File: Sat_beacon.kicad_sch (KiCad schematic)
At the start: 131 parts, among them IC1 LMX2581ESQE_NOPB, IC2 LMX2581ESQE_NOPB, J1 Conn_01x05_Pin, J2 Conn_01x05_Pin, J3 Conn_01x03_Pin, J4 MMCX, J5 MMCX, Q1 BC817-40, Q2 BC817-40, Q3 BC817-40, Q4 BC817-40, SW1 SW_SPDT_312, SW2 SW_Omron_B3FS, SW3 SW_Omron_B3FS, SW4 SW_Omron_B3FS, SW5 SW_Omron_B3FS, U1 STM32C011F6Px, U2 LD1117DT33, U3 LD1117DT33, U4 1720BL15B0050002E, U5 1720BL15B0050002E, U6 LD1117DT33, U7 STM32C031C6Tx, Y1 FT2MHUPM10.0-T1

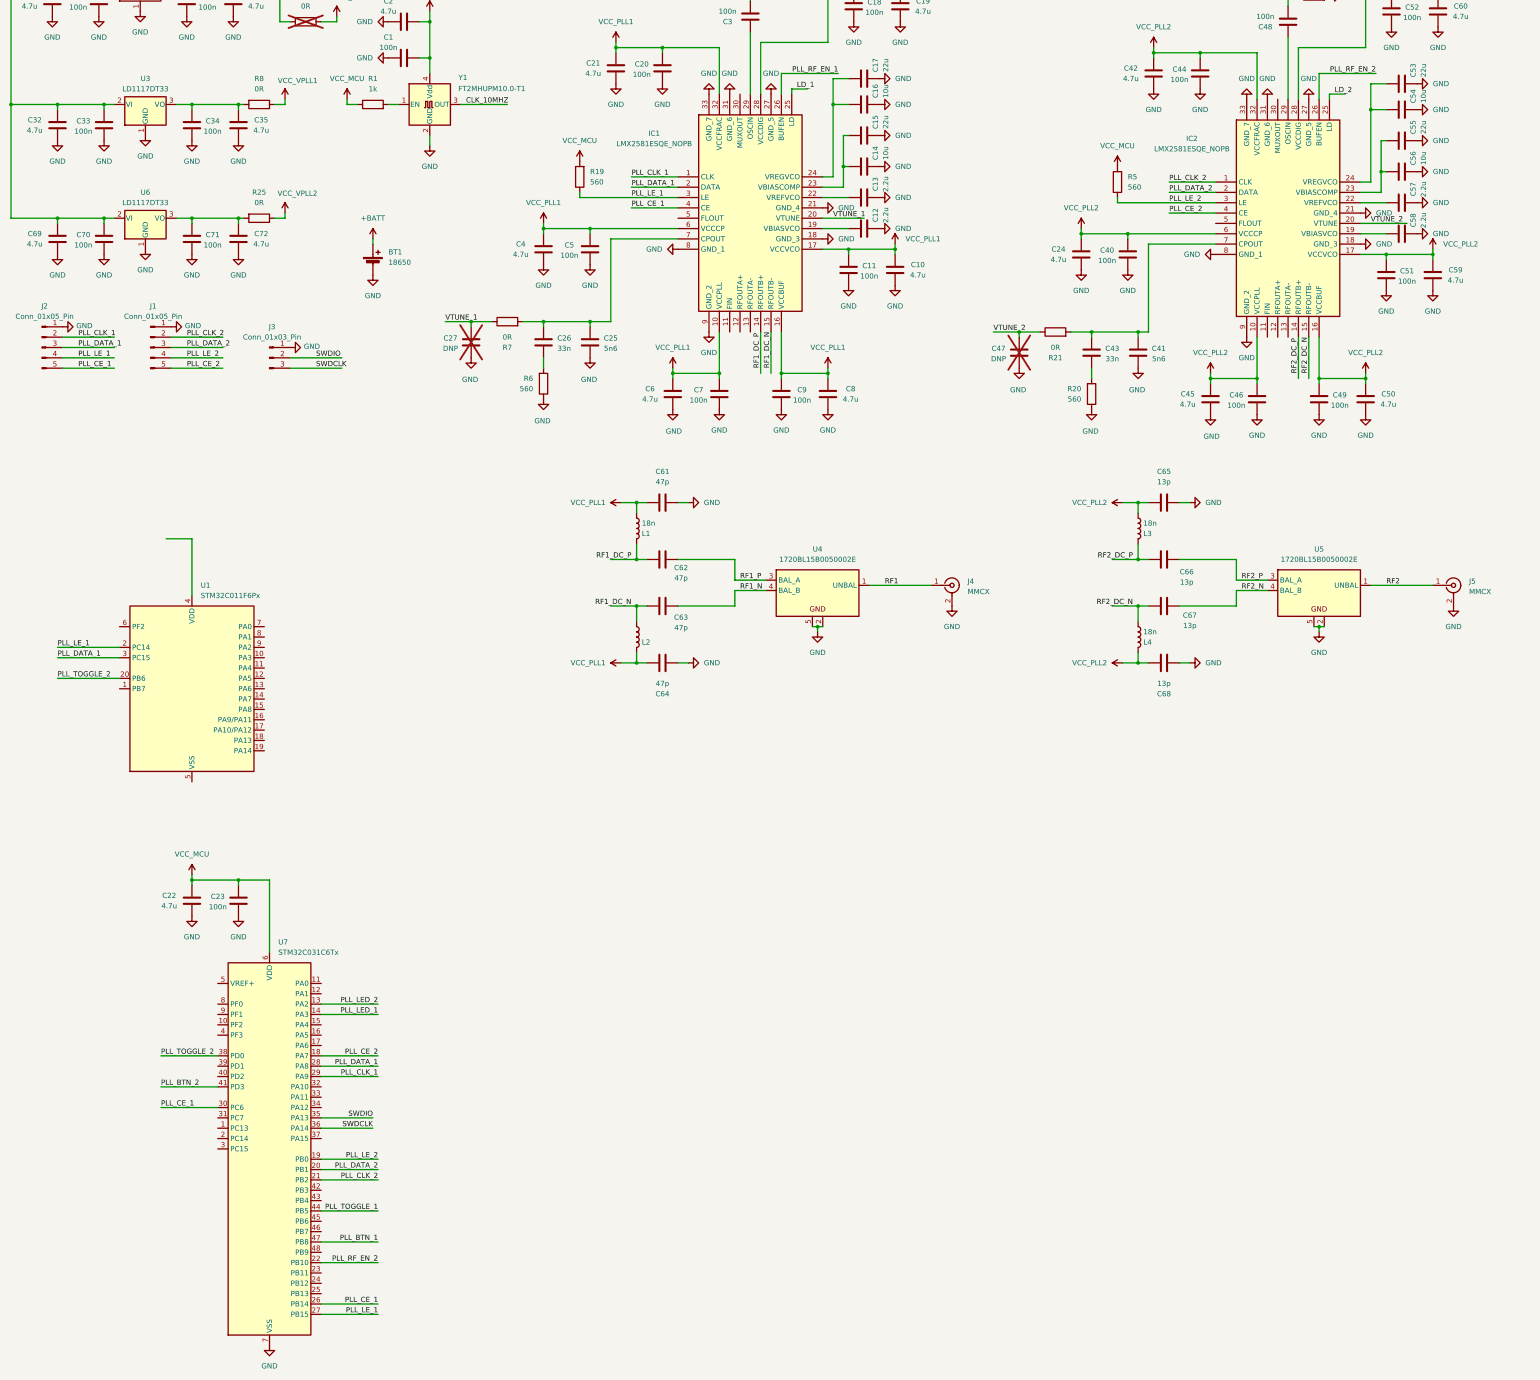
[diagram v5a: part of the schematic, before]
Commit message: Group and place components on PCB, two PLL caps removed, swapped RF lines
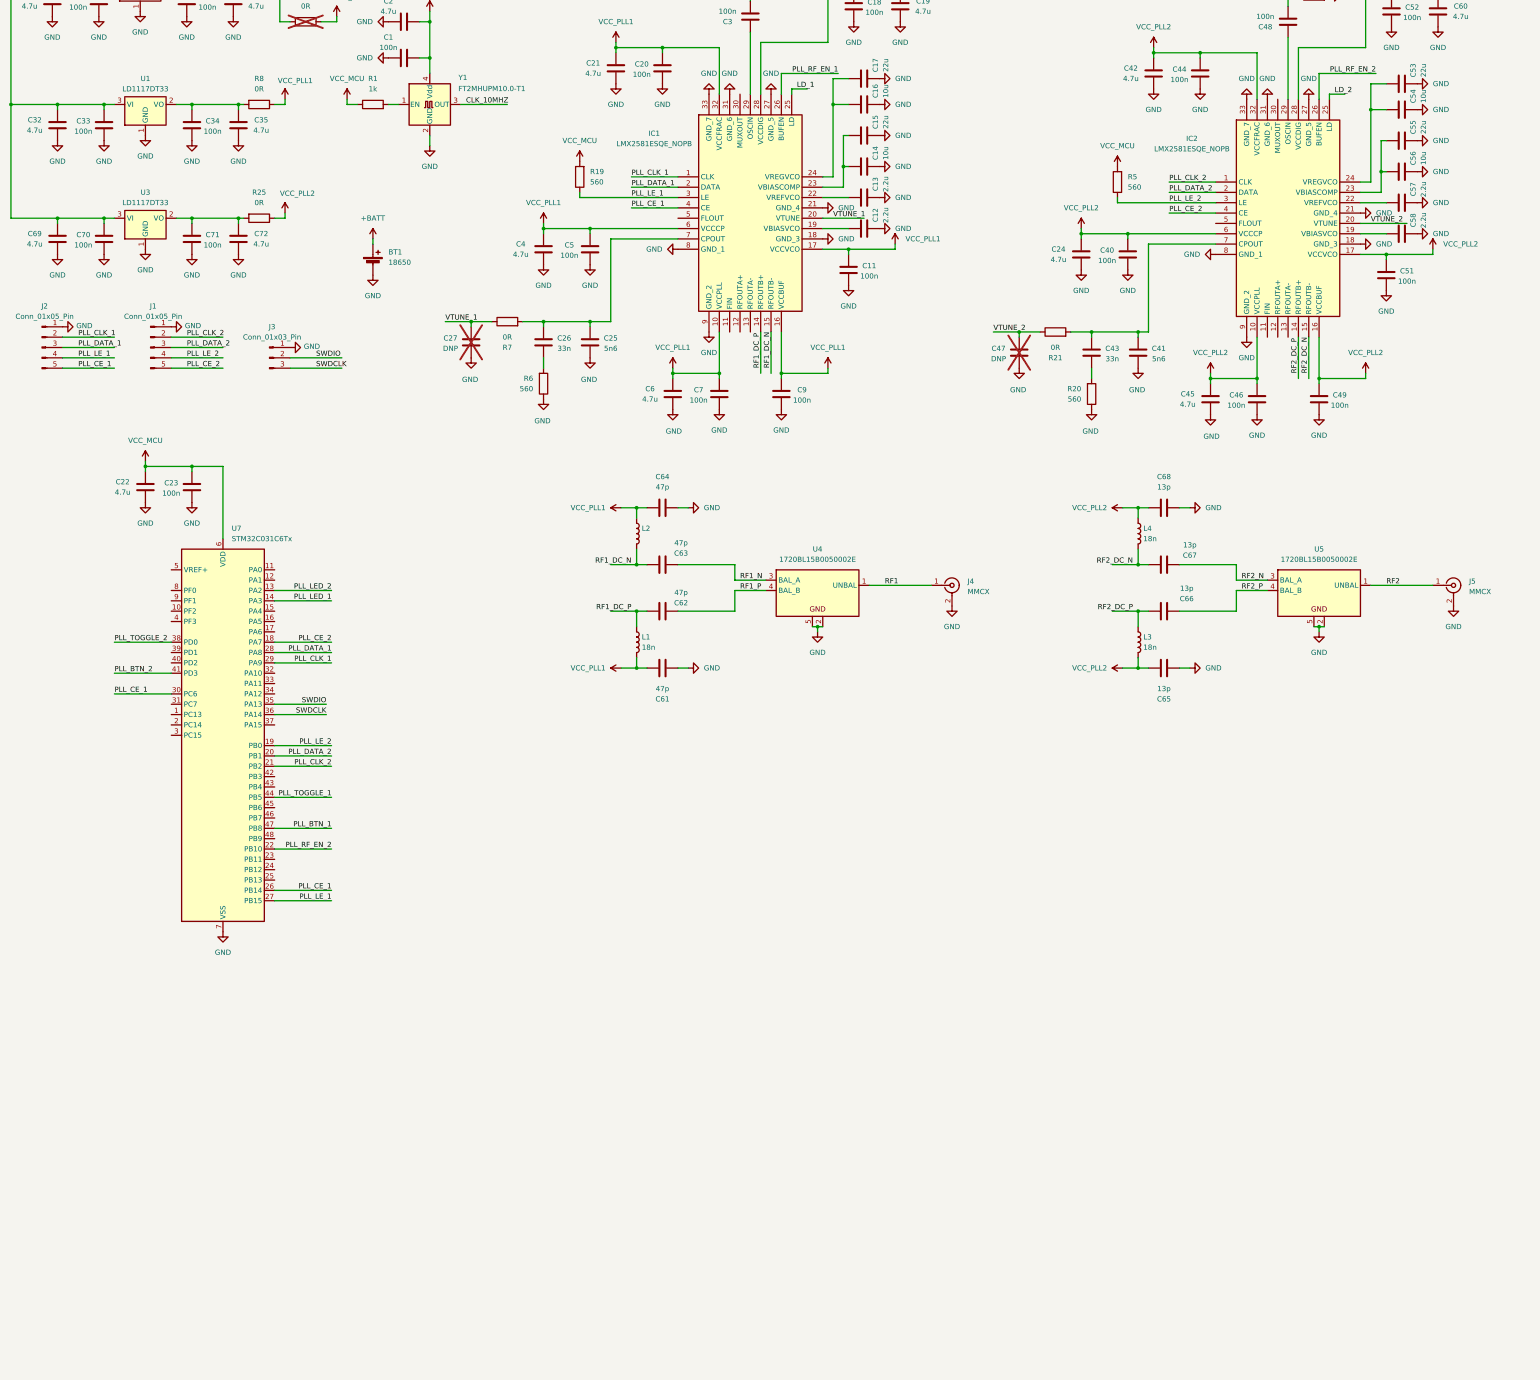
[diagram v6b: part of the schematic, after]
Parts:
- removed C10, C50, C59, C8: 4.7u, Capacitor_SMD:C_0805_2012Metric, symbol Device:C
- removed U1: STM32C011F6Px, Package_SO:TSSOP-20_4.4x6.5mm_P0.65mm, symbol MCU_ST_STM32C0:STM32C011F6Px
- removed U3, U6: LD1117DT33, Package_TO_SOT_THT:TO-220-3_Vertical, symbol Regulator_Linear:MCP1700x-330xxMB
- added U1, U3: LD1117DT33, Package_TO_SOT_SMD:TO-252-3_TabPin2, symbol Regulator_Linear:LD1117V33
- U2: footprint Package_TO_SOT_THT:TO-220-3_Vertical -> Package_TO_SOT_SMD:TO-252-3_TabPin2
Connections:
- net VCC_VPLL1 is gone; now on net VCC_PLL1: R8.1
- net VCC_VPLL2 is gone; now on net VCC_PLL2: R25.1
- net GND: now also U1.1 (GND), U3.1 (GND)
- net RF1_N: now also U4.3 (BAL_A); no longer U4.4 (BAL_B)
- net RF1_P: now also U4.4 (BAL_B); no longer U4.3 (BAL_A)
- net RF2_N: now also U5.3 (BAL_A); no longer U5.4 (BAL_B)
- net RF2_P: now also U5.4 (BAL_B); no longer U5.3 (BAL_A)
- net at C28.2, C29.2, C32.2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: now also U1.3 (VI), U3.3 (VI)
- net at C71.2, C72.2, R25.2: now also U3.2 (VO)
- net at C34.2, C35.2, R8.2: now also U1.2 (VO)
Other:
- moved on the sheet: C22, C23, C61, C62, C63, C64, C65, C66, C67, C68, L1, L2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

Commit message: MUXout added, LEDs swapped (SCH only)
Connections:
- net PLL_CE_1: no longer U7.30 (PC6)
- net PLL_LED_1: now also R18.1, U7.13 (PA2); no longer R16.1, U7.14 (PA3)
- net PLL_LED_2: now also R16.1, U7.14 (PA3); no longer R18.1, U7.13 (PA2)
- net PLL_RF_EN_1: now also U7.31 (PC7)
- net PLL_RF_EN_2: now also U7.23 (PB11); no longer U7.22 (PB10)
- net PLL_MUXOUT_1: now reaches IC1.30 (MUXOUT)
- net PLL_MUXOUT_2: now reaches IC2.30 (MUXOUT)
- new net PLL_MUXout_1: U7.30 (PC6)
- new net PLL_MUXout_2: U7.22 (PB10)
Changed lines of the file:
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@@
 	(wire
 		(pts
+			(xy 81.28 252.73) (xy 95.25 252.73)
+		)
+		(stroke
+			(width 0)
+			(type default)
+		)
+	)
+	(wire
+		(pts
 			(xy 198.12 39.37) (xy 200.66 39.37)
 		)
@@
 	(wire
 		(pts
+			(xy 327.66 52.07) (xy 327.66 66.04)
+		)
+		(stroke
+			(width 0)
+			(type default)
+		)
+	)
+	(wire
+		(pts
 			(xy 27.94 95.25) (xy 39.37 95.25)
 		)
@@
 	(wire
 		(pts
+			(xy 176.53 50.8) (xy 195.58 50.8)
+		)
+		(stroke
+			(width 0)
+			(type default)
+		)
+	)
+	(wire
+		(pts
 			(xy 337.82 124.46) (xy 337.82 134.62)
 		)
@@
 	(wire
 		(pts
+			(xy 41.91 214.63) (xy 55.88 214.63)
+		)
+		(stroke
+			(width 0)
+			(type default)
+		)
+	)
+	(wire
+		(pts
 			(xy 55.88 127) (xy 68.58 127)
 		)
@@
 	(wire
 		(pts
+			(xy 195.58 50.8) (xy 195.58 64.77)
+		)
+		(stroke
+			(width 0)
+			(type default)
+		)
+	)
+	(wire
+		(pts
 			(xy 317.5 184.15) (xy 325.12 184.15)
 		)
@@
 	(wire
 		(pts
+			(xy 308.61 52.07) (xy 327.66 52.07)
+		)
+		(stroke
+			(width 0)
+			(type default)
+		)
+	)
+	(wire
+		(pts
 			(xy 426.72 176.53) (xy 426.72 180.34)
 		)
@@
 		)
 	)
-	(label "PLL_LED_1"
+	(label "PLL_LED_2"
 		(at 449.58 135.89 0)
 		(effects
@@
 		)
 	)
+	(label "PLL_RF_EN_1"
+		(at 41.91 214.63 0)
+		(effects
+			(font
+				(size 1.27 1.27)
+			)
+			(justify left bottom)
+		)
+	)
 	(label "VTUNE_1"
 		(at 218.44 95.25 0)
@@
 		)
 	)
-	(label "PLL_LED_2"
+	(label "PLL_LED_1"
 		(at 449.58 185.42 0)
 		(effects
@@
 		)
 	)
-	(label "PLL_LED_1"
+	(label "PLL_LED_2"
 		(at 95.25 189.23 180)
 		(effects
@@
 		)
 	)
-	(label "PLL_RF_EN_2"
+	(label "PLL_MUXout_2"
 		(at 95.25 250.19 180)
 		(effects
@@
 		)
 	)
-	(label "PLL_LED_2"
+	(label "PLL_LED_1"
 		(at 95.25 186.69 180)
 		(effects
@@
 		)
 	)
-	(label "PLL_CE_1"
+	(label "PLL_MUXout_1"
 		(at 41.91 212.09 0)
 		(effects
@@
 		)
 	)
+	(label "PLL_RF_EN_2"
+		(at 95.25 252.73 180)
+		(effects
+			(font
+				(size 1.27 1.27)
+			)
+			(justify right bottom)
+		)
+	)
+	(label "PLL_MUXOUT_2"
+		(at 308.61 52.07 0)
+		(effects
+			(font
+				(size 1.27 1.27)
+			)
+			(justify left bottom)
+		)
+	)
 	(label "PLL_CLK_1"
 		(at 95.25 204.47 180)
@@
 		(effects
 			(font
+				(size 1.27 1.27)
+			)
+			(justify left bottom)
+		)
+	)
+	(label "PLL_MUXOUT_1"
+		(at 176.53 50.8 0)
+		(effects
+			(font

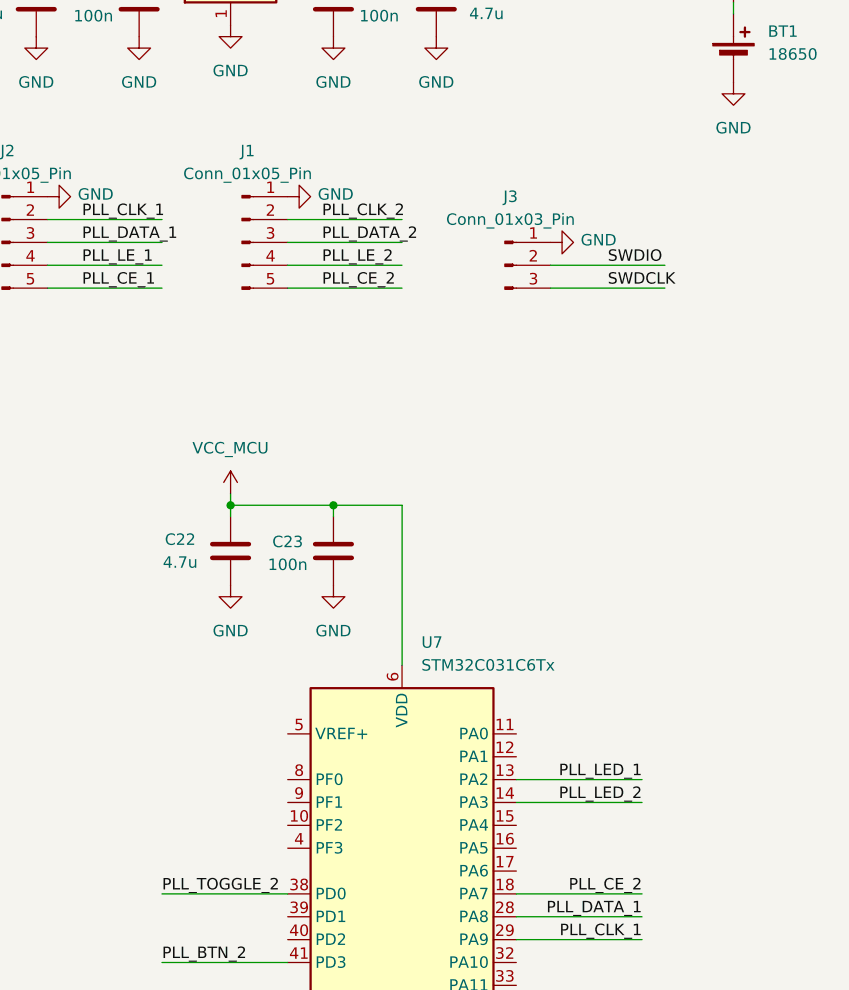
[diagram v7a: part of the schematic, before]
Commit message: NRST pin added
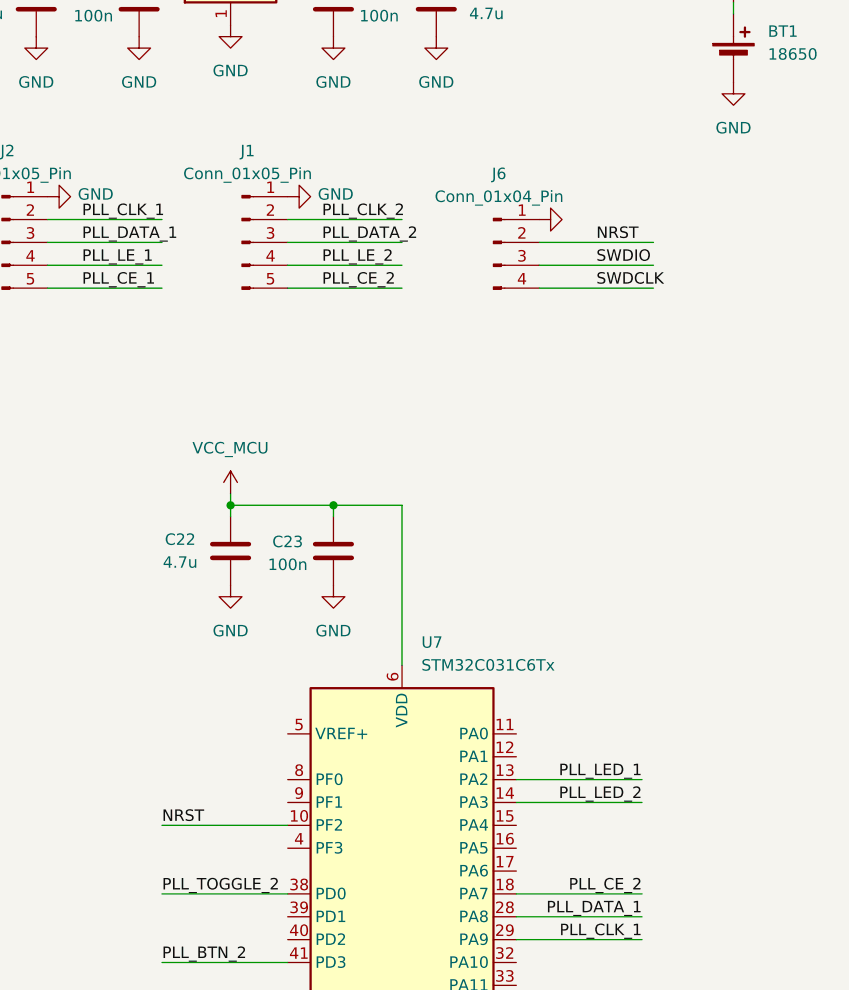
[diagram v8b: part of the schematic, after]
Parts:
- removed J3: Conn_01x03_Pin, Connector_PinHeader_2.54mm:PinHeader_1x03_P2.54mm_Vertical, symbol Connector:Conn_01x03_Pin
- added J6: Conn_01x04_Pin, symbol Connector:Conn_01x04_Pin
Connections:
- net GND: now also J6.1 (Pin_1)
- net SWDCLK: now also J6.4 (Pin_4)
- net SWDIO: now also J6.3 (Pin_3)
- net NRST: now reaches U7.10 (PF2)
- net NRST: now also J6.2 (Pin_2)
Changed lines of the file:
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@@
 	(wire
 		(pts
+			(xy 83.82 132.08) (xy 96.52 132.08)
+		)
+		(stroke
+			(width 0)
+			(type default)
+		)
+	)
+	(wire
+		(pts
 			(xy 295.91 101.6) (xy 295.91 123.19)
 		)
@@
 	(wire
 		(pts
-			(xy 85.09 129.54) (xy 97.79 129.54)
-		)
-		(stroke
-			(width 0)
-			(type default)
-		)
-	)
-	(wire
-		(pts
 			(xy 439.42 73.66) (xy 439.42 74.93)
 		)
@@
 	(wire
 		(pts
+			(xy 83.82 129.54) (xy 96.52 129.54)
+		)
+		(stroke
+			(width 0)
+			(type default)
+		)
+	)
+	(wire
+		(pts
 			(xy 55.88 132.08) (xy 68.58 132.08)
 		)
@@
 	(wire
 		(pts
+			(xy 83.82 127) (xy 96.52 127)
+		)
+		(stroke
+			(width 0)
+			(type default)
+		)
+	)
+	(wire
+		(pts
 			(xy 276.86 123.19) (xy 281.94 123.19)
 		)
@@
 	(wire
 		(pts
+			(xy 41.91 191.77) (xy 55.88 191.77)
+		)
+		(stroke
+			(width 0)
+			(type default)
+		)
+	)
+	(wire
+		(pts
 			(xy 233.68 102.87) (xy 222.25 102.87)
 		)
@@
 	(wire
 		(pts
+			(xy 41.91 199.39) (xy 55.88 199.39)
+		)
+		(stroke
+			(width 0)
+			(type default)
+		)
+	)
+	(wire
+		(pts
 			(xy 119.38 44.45) (xy 119.38 46.99)
 		)
@@
 	(wire
 		(pts
-			(xy 41.91 199.39) (xy 55.88 199.39)
-		)
-		(stroke
-			(width 0)
-			(type default)
-		)
-	)
-	(wire
-		(pts
 			(xy 156.21 88.9) (xy 156.21 90.17)
 		)
@@
 	(wire
 		(pts
-			(xy 85.09 132.08) (xy 97.79 132.08)
-		)
-		(stroke
-			(width 0)
-			(type default)
-		)
-	)
-	(wire
-		(pts
 			(xy 416.56 135.89) (xy 419.1 135.89)
 		)
@@
 		)
 	)
-	(label "SWDCLK"
-		(at 91.44 132.08 0)
+	(label "NRST"
+		(at 41.91 191.77 0)
 		(effects
 			(font
@@
 		)
 	)
-	(label "PLL_LE_2"
-		(at 300.99 91.44 0)
+	(label "SWDIO"
+		(at 90.17 129.54 0)
 		(effects
 			(font
@@
 		)
 	)
-	(label "PLL_TOGGLE_2"
-		(at 461.01 74.93 0)
+	(label "PLL_LE_2"
+		(at 300.99 91.44 0)
 		(effects
 			(font
@@
 	)
 	(label "PLL_TOGGLE_2"
-		(at 41.91 199.39 0)
+		(at 461.01 74.93 0)
 		(effects
 			(font
@@
 		)
 	)
-	(label "PLL_BTN_1"
-		(at 422.91 36.83 0)
+	(label "PLL_TOGGLE_2"
+		(at 41.91 199.39 0)
 		(effects
 			(font
@@
 		)
 	)
-	(label "LD_2"
-		(at 341.63 64.77 0)
+	(label "PLL_BTN_1"
+		(at 422.91 36.83 0)
 		(effects
 			(font
@@
 		)
 	)
-	(label "RF2_N"
-		(at 318.77 184.15 0)
+	(label "LD_2"
+		(at 341.63 64.77 0)
 		(effects
 			(font
@@
 		)
 	)
-	(label "SWDIO"
-		(at 91.44 129.54 0)
+	(label "RF2_N"
+		(at 318.77 184.15 0)
 		(effects
 			(font
@@
 		)
 	)
+	(label "SWDCLK"
+		(at 90.17 132.08 0)
+		(effects
+			(font
+				(size 1.27 1.27)
+			)
+			(justify left bottom)
+		)
+	)
 	(label "RF1_DC_N"
 		(at 168.91 180.34 180)
@@
 		)
 	)
+	(label "NRST"
+		(at 90.17 127 0)
+		(effects
+			(font
+				(size 1.27 1.27)
+			)
+			(justify left bottom)
+		)
+	)
 	(symbol
 		(lib_id "power:GND")
@@
 	)
 	(symbol
+		(lib_id "Connector:Conn_01x04_Pin")
+		(at 78.74 127 0)
+		(unit 1)
+		(exclude_from_sim no)
+		(in_bom yes)
+		(on_board yes)
+		(dnp no)
+		(fields_autoplaced yes)
+		(property "Reference" "J6"
+			(at 79.375 119.38 0)
+			(effects
+				(font
+					(size 1.27 1.27)
+				)
+			)
+		)
+		(property "Value" "Conn_01x04_Pin"
+			(at 79.375 121.92 0)
+			(effects
+				(font
+					(size 1.27 1.27)
+				)
+			)
+		)
+		(property "Footprint" ""
+			(at 78.74 127 0)
+			(effects
+				(font
+					(size 1.27 1.27)
+				)
+				(hide yes)
+			)
+		)
+		(property "Datasheet" "~"
+			(at 78.74 127 0)
+			(effects
+				(font
+					(size 1.27 1.27)
+				)
+				(hide yes)
+			)
+		)
+		(property "Description" "Generic connector, single row, 01x04, script generated"
+			(at 78.74 127 0)
+			(effects
+				(font
+					(size 1.27 1.27)
+				)
+				(hide yes)
+			)
+		)
+		(pin "3"
+		)
+		(pin "4"
+		)
+		(pin "1"
+		)
+		(pin "2"
+		)
+		(instances
+			(project ""
+				(path "/d50b57a8-fbd1-4b9f-a519-640b54fbccac"
+					(reference "J6")
+					(unit 1)
+				)
+			)
+		)
+	)
+	(symbol
 		(lib_id "Device:C")
 		(at 279.4 104.14 180)
@@
 	(symbol
 		(lib_id "power:GND")
-		(at 85.09 127 90)
+		(at 83.82 124.46 90)
 		(unit 1)
 		(exclude_from_sim no)
@@
 		(dnp no)
 		(property "Reference" "#PWR069"
-			(at 91.44 127 0)
+			(at 90.17 124.46 0)
 			(effects
 				(font
@@
 		)
 		(property "Value" "GND"
-			(at 90.424 126.746 90)
+			(at 89.154 124.206 90)
 			(effects
 				(font
 					(size 1.27 1.27)
 				)
+				(hide yes)
 			)
 		)
 		(property "Footprint" ""
-			(at 85.09 127 0)
+			(at 83.82 124.46 0)
 			(effects
 				(font
@@
 		)
 		(property "Datasheet" ""
-			(at 85.09 127 0)
+			(at 83.82 124.46 0)
 			(effects
 				(font
@@
 		)
 		(property "Description" "Power symbol creates a global label with name \"GND\" , ground"
-			(at 85.09 127 0)
+			(at 83.82 124.46 0)
 			(effects
 				(font
@@
 					(unit 1)
 				)
-			)
-		)
-	)
-	(symbol
-		(lib_id "Connector:Conn_01x03_Pin")
-		(at 80.01 129.54 0)
-		(unit 1)
-		(exclude_from_sim no)
-		(in_bom yes)
-		(on_board yes)
-		(dnp no)
-		(fields_autoplaced yes)
-		(property "Reference" "J3"
-			(at 80.645 121.92 0)
-			(effects
-				(font
-					(size 1.27 1.27)
-				)
-			)
-		)
-		(property "Value" "Conn_01x03_Pin"
-			(at 80.645 124.46 0)
-			(effects
-				(font
-					(size 1.27 1.27)
-				)
-			)
-		)
-		(property "Footprint" "Connector_PinHeader_2.54mm:PinHeader_1x03_P2.54mm_Vertical"
-			(at 80.01 129.54 0)
-			(effects
-				(font
-					(size 1.27 1.27)
-				)
-				(hide yes)
-			)
-		)
-		(property "Datasheet" "~"
-			(at 80.01 129.54 0)
-			(effects
-				(font
-					(size 1.27 1.27)
-				)
-				(hide yes)
-			)
-		)
-		(property "Description" "Generic connector, single row, 01x03, script generated"
-			(at 80.01 129.54 0)
-			(effects
-				(font
-					(size 1.27 1.27)
-				)
-				(hide yes)
-			)
-		)
-		(pin "1"
-		)
-		(pin "3"
-		)
-		(pin "2"
-		)
-		(instances
-			(project "Sat_beacon"
-				(path "/d50b57a8-fbd1-4b9f-a519-640b54fbccac"
-					(reference "J3")
-					(unit 1)
-				)
